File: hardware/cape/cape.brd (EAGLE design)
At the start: 86.4 x 54.6 mm, 159 parts, among them IC1 AD8422BRMZ, IC10 DAC8562_DGS_10, IC11 CAT24C256WI-GT3, IC12 LM27762DSSR, IC13 BQ25505, IC14 SN74LV4T125PWR, IC15 LMP7701MF, IC16 TXB0304RUTR, IC2 OPA2388DGK8_L, IC3 AD8422BRMZ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

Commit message: hardware: fixed wrong part number for constant supply LDO
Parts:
- IC8: value TPS73125DBVR -> TPS73101DBVR; device mylib:SOT95P280X145-5N -> shepherd:SOT95P280X145-5N
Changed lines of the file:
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@@
 <attribute name="VALUE" x="29.591" y="21.442" size="1.27" layer="27" rot="R180" align="top-center"/>
 </element>
-<element name="IC8" library="mylib" package="SOT95P280X145-5N" value="TPS73125DBVR" x="49.403" y="33.782" smashed="yes" rot="R180">
+<element name="IC8" library="shepherd" package="SOT95P280X145-5N" value="TPS73101DBVR" x="49.403" y="33.782" smashed="yes" rot="R180">
 <attribute name="AVAILABILITY" value="Unavailable" x="49.403" y="33.782" size="1.778" layer="27" rot="R180" display="off"/>
 <attribute name="DESCRIPTION" value=" Cap-Free, NMOS, 150mA Low Dropout Regulator with Reverse Current Protection 5-SOT-23 -40 to 125 " x="49.403" y="33.782" size="1.778" layer="27" rot="R180" display="off"/>
 <attribute name="MF" value="Texas Instruments" x="49.403" y="33.782" size="1.778" layer="27" rot="R180" display="off"/>
-<attribute name="MP" value="TPS73125DBVR" x="49.403" y="33.782" size="1.778" layer="27" rot="R180" display="off"/>
+<attribute name="MP" value="TPS73101DBVR" x="49.403" y="33.782" size="1.778" layer="27" rot="R180" display="off"/>
 <attribute name="NAME" x="49.62795" y="35.435690625" size="0.8128" layer="25" font="vector" ratio="15" rot="SR0"/>
 <attribute name="PACKAGE" value="SOT-23-5 Texas Instruments" x="49.403" y="33.782" size="1.778" layer="27" rot="R180" display="off"/>

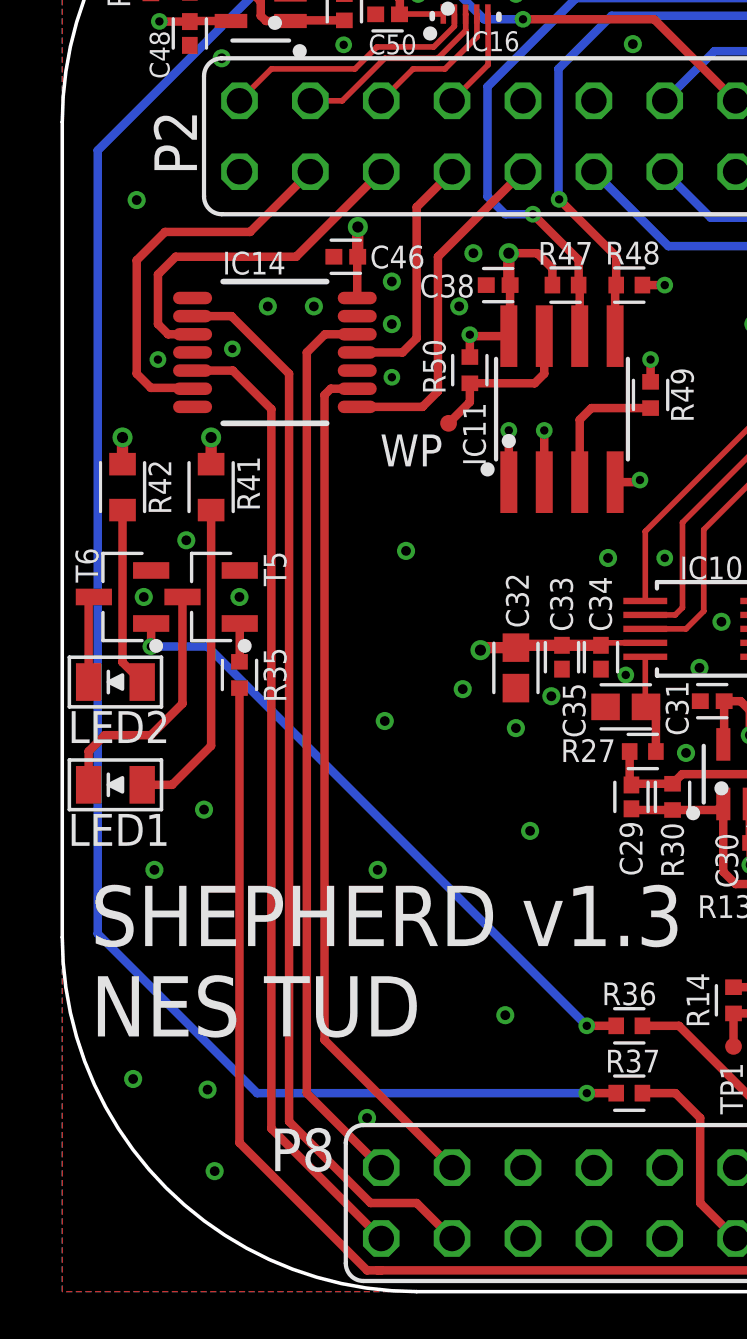
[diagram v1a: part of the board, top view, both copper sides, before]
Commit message: hardware: fixed direction of level-converter
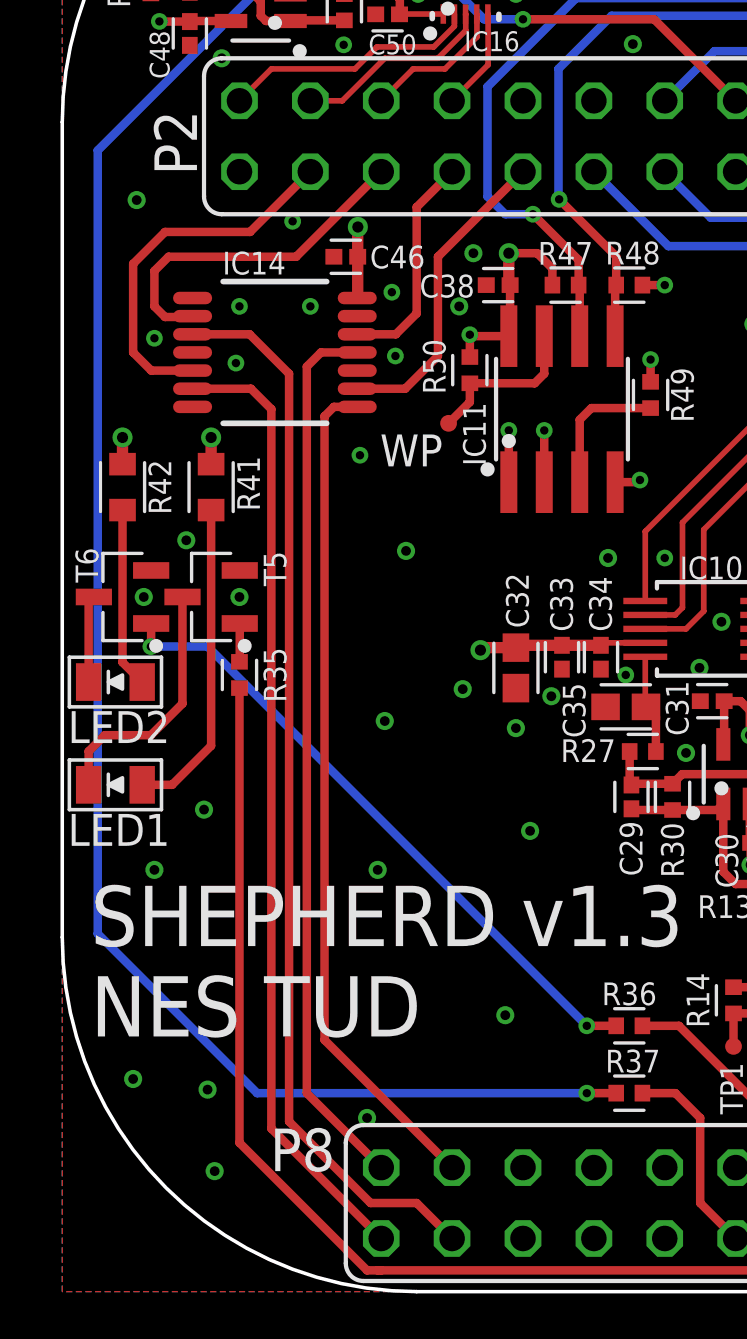
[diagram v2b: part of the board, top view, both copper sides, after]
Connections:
- net GPIO0_BB: now also IC14.11; no longer IC14.12
- net GPIO0_TARGET: now also IC14.12; no longer IC14.11
- net GPIO1_BB: now also IC14.6; no longer IC14.5
- net GPIO1_TARGET: now also IC14.5; no longer IC14.6
- net GPIO2_BB: now also IC14.8; no longer IC14.9
- net GPIO2_TARGET: now also IC14.9; no longer IC14.8
- net GPIO3_BB: now also IC14.3; no longer IC14.2
- net GPIO3_TARGET: now also IC14.2; no longer IC14.3
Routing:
- net GPIO2_TARGET: track 12.3 -> 11.2 mm
- net GPIO0_TARGET: track 8.84 -> 8.05 mm
- net GPIO2_BB: track 30.8 -> 30.1 mm
- net GPIO0_BB: track 32.4 -> 31.8 mm
- net GPIO1_TARGET: track 13.8 -> 13.3 mm
- net GND: vias 154 -> 155
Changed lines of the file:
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@@
 <via x="32.131" y="21.971" extent="1-16" drill="0.35"/>
 <via x="25.654" y="27.051" extent="1-16" drill="0.35" alwaysstop="yes"/>
-<via x="9.017" y="35.306" extent="1-16" drill="0.35"/>
-<via x="7.366" y="35.306" extent="1-16" drill="0.35"/>
-<via x="11.811" y="36.195" extent="1-16" drill="0.35"/>
-<via x="11.811" y="34.671" extent="1-16" drill="0.35"/>
 <via x="20.447" y="44.704" extent="1-16" drill="0.35"/>
 <via x="29.083" y="36.195" extent="1-16" drill="0.35"/>
@@
 <via x="57.912" y="15.24" extent="1-16" drill="0.3"/>
 <via x="60.96" y="15.24" extent="1-16" drill="0.3"/>
-<via x="3.429" y="33.401" extent="1-16" drill="0.3"/>
-<via x="11.811" y="32.766" extent="1-16" drill="0.3"/>
-<via x="6.096" y="33.782" extent="1-16" drill="0.3"/>
 <via x="6.35" y="24.892" extent="1-16" drill="0.35"/>
 <via x="2.921" y="24.892" extent="1-16" drill="0.35"/>
@@
 <via x="9.3218" y="49.911" extent="1-16" drill="0.3"/>
 <via x="5.715" y="44.196" extent="1-16" drill="0.35"/>
+<via x="6.35" y="35.306" extent="1-16" drill="0.3"/>
+<via x="8.89" y="35.306" extent="1-16" drill="0.3"/>
+<via x="6.223" y="33.274" extent="1-16" drill="0.3"/>
+<via x="3.302" y="34.163" extent="1-16" drill="0.3"/>
+<via x="10.668" y="29.972" extent="1-16" drill="0.3"/>
+<via x="11.938" y="33.528" extent="1-16" drill="0.3"/>
+<via x="11.811" y="35.814" extent="1-16" drill="0.3"/>
+<via x="8.255" y="38.354" extent="1-16" drill="0.3"/>
 </signal>
 <signal name="V_H">
@@
 <contactref element="C46" pad="1"/>
 <contactref element="IC14" pad="14"/>
-<wire x1="10.57" y1="35.605" x2="10.57" y2="37.0671" width="0.3048" layer="1"/>
 <wire x1="10.57" y1="37.0671" x2="10.5869" y2="37.084" width="0.3048" layer="1"/>
 <wire x1="10.5869" y1="37.084" x2="10.5869" y2="38.1459" width="0.4064" layer="1"/>
@@
 <wire x1="12.0855" y1="48.6615" x2="12.7" y2="49.276" width="0.3048" layer="1"/>
 <via x="12.7" y="49.276" extent="1-16" drill="0.3"/>
+<wire x1="10.5869" y1="37.084" x2="10.5869" y2="35.6219" width="0.4064" layer="1"/>
+<wire x1="10.5869" y1="35.6219" x2="10.57" y2="35.605" width="0.4064" layer="1"/>
 </signal>
 <signal name="N$3">
@@
 <signal name="GPIO0_BB">
 <contactref element="P8" pad="45"/>
-<contactref element="IC14" pad="12"/>
-<wire x1="10.57" y1="34.305" x2="9.413" y2="34.305" width="0.3048" layer="1"/>
-<wire x1="8.763" y1="7.112" x2="11.43" y2="4.445" width="0.3048" layer="1"/>
-<wire x1="9.413" y1="34.305" x2="8.763" y2="33.655" width="0.3048" layer="1"/>
-<wire x1="8.763" y1="33.655" x2="8.763" y2="7.112" width="0.3048" layer="1"/>
+<wire x1="11.43" y1="4.445" x2="8.763" y2="7.112" width="0.3048" layer="1"/>
+<contactref element="IC14" pad="11"/>
+<wire x1="8.763" y1="7.112" x2="8.763" y2="33.147" width="0.3048" layer="1"/>
+<wire x1="8.763" y1="33.147" x2="9.271" y2="33.655" width="0.3048" layer="1"/>
+<wire x1="9.271" y1="33.655" x2="10.57" y2="33.655" width="0.3048" layer="1"/>
 </signal>
 <signal name="GPIO1_BB">
 <contactref element="P8" pad="46"/>
-<contactref element="IC14" pad="5"/>
 <wire x1="7.493" y1="5.842" x2="11.43" y2="1.905" width="0.3048" layer="1"/>
-<wire x1="4.669996875" y1="33.005" x2="6.111" y2="33.005" width="0.3048" layer="1"/>
-<wire x1="6.111" y1="33.005" x2="7.493" y2="31.623" width="0.3048" layer="1"/>
-<wire x1="7.493" y1="31.623" x2="7.493" y2="5.842" width="0.3048" layer="1"/>
+<wire x1="7.493" y1="5.842" x2="7.493" y2="31.623" width="0.3048" layer="1"/>
+<contactref element="IC14" pad="6"/>
+<wire x1="7.493" y1="31.623" x2="6.761" y2="32.355" width="0.3048" layer="1"/>
+<wire x1="6.761" y1="32.355" x2="4.669996875" y2="32.355" width="0.3048" layer="1"/>
 </signal>
 <signal name="GPIO2_BB">
 <contactref element="P8" pad="43"/>
-<contactref element="IC14" pad="9"/>
-<wire x1="9.622" y1="32.355" x2="10.57" y2="32.355" width="0.3048" layer="1"/>
 <wire x1="13.97" y1="4.445" x2="9.398" y2="9.017" width="0.3048" layer="1"/>
-<wire x1="9.398" y1="9.017" x2="9.398" y2="32.131" width="0.3048" layer="1"/>
-<wire x1="9.398" y1="32.131" x2="9.622" y2="32.355" width="0.3048" layer="1"/>
+<contactref element="IC14" pad="8"/>
+<wire x1="9.398" y1="9.017" x2="9.398" y2="31.369" width="0.3048" layer="1"/>
+<wire x1="9.734" y1="31.705" x2="10.57" y2="31.705" width="0.3048" layer="1"/>
+<wire x1="9.398" y1="31.369" x2="9.734" y2="31.705" width="0.3048" layer="1"/>
 </signal>
 <signal name="GPIO3_BB">
 <contactref element="P8" pad="44"/>
-<contactref element="IC14" pad="2"/>
-<wire x1="4.669996875" y1="34.955" x2="6.066" y2="34.955" width="0.3048" layer="1"/>
-<wire x1="6.066" y1="34.955" x2="8.128" y2="32.893" width="0.3048" layer="1"/>
 <wire x1="8.128" y1="6.096" x2="11.049" y2="3.175" width="0.3048" layer="1"/>
 <wire x1="11.049" y1="3.175" x2="12.7" y2="3.175" width="0.3048" layer="1"/>
 <wire x1="12.7" y1="3.175" x2="13.97" y2="1.905" width="0.3048" layer="1"/>
-<wire x1="8.128" y1="32.893" x2="8.128" y2="6.096" width="0.3048" layer="1"/>
+<wire x1="8.128" y1="6.096" x2="8.128" y2="32.893" width="0.3048" layer="1"/>
+<contactref element="IC14" pad="3"/>
+<wire x1="8.128" y1="32.893" x2="6.716" y2="34.305" width="0.3048" layer="1"/>
+<wire x1="6.716" y1="34.305" x2="4.669996875" y2="34.305" width="0.3048" layer="1"/>
 </signal>
 <signal name="GPIO0_TARGET">
 <contactref element="P2" pad="10"/>
-<contactref element="IC14" pad="11"/>
-<wire x1="10.57" y1="33.655" x2="12.192" y2="33.655" width="0.3048" layer="1"/>
-<wire x1="12.192" y1="33.655" x2="12.7" y2="34.163" width="0.3048" layer="1"/>
-<wire x1="12.7" y1="34.163" x2="12.7" y2="38.862" width="0.3048" layer="1"/>
-<wire x1="12.7" y1="38.862" x2="13.97" y2="40.132" width="0.3048" layer="1"/>
+<wire x1="13.97" y1="40.132" x2="12.7" y2="38.862" width="0.3048" layer="1"/>
+<contactref element="IC14" pad="12"/>
+<wire x1="11.953" y1="34.305" x2="10.57" y2="34.305" width="0.3048" layer="1"/>
+<wire x1="12.7" y1="38.862" x2="12.7" y2="35.052" width="0.3048" layer="1"/>
+<wire x1="12.7" y1="35.052" x2="11.953" y2="34.305" width="0.3048" layer="1"/>
 </signal>
 <signal name="GPIO1_TARGET">
 <contactref element="P2" pad="14"/>
-<contactref element="IC14" pad="6"/>
 <wire x1="8.89" y1="40.132" x2="6.731" y2="37.973" width="0.3048" layer="1"/>
-<wire x1="3.683" y1="37.973" x2="2.667" y2="36.957" width="0.3048" layer="1"/>
-<wire x1="2.667" y1="36.957" x2="2.667" y2="32.893" width="0.3048" layer="1"/>
-<wire x1="2.667" y1="32.893" x2="3.175" y2="32.385" width="0.3048" layer="1"/>
-<wire x1="3.175" y1="32.385" x2="4.639996875" y2="32.385" width="0.3048" layer="1"/>
-<wire x1="4.639996875" y1="32.385" x2="4.669996875" y2="32.355" width="0.3048" layer="1"/>
+<wire x1="3.683" y1="37.973" x2="2.54" y2="36.83" width="0.3048" layer="1"/>
 <wire x1="6.731" y1="37.973" x2="3.683" y2="37.973" width="0.3048" layer="1"/>
+<contactref element="IC14" pad="5"/>
+<wire x1="2.54" y1="36.83" x2="2.54" y2="33.655" width="0.3048" layer="1"/>
+<wire x1="3.19" y1="33.005" x2="4.669996875" y2="33.005" width="0.3048" layer="1"/>
+<wire x1="2.54" y1="33.655" x2="3.19" y2="33.005" width="0.3048" layer="1"/>
 </signal>
 <signal name="GPIO2_TARGET">
 <contactref element="P2" pad="8"/>
-<contactref element="IC14" pad="8"/>
-<wire x1="10.57" y1="31.705" x2="12.909" y2="31.705" width="0.3048" layer="1"/>
-<wire x1="12.909" y1="31.705" x2="13.462" y2="32.258" width="0.3048" layer="1"/>
-<wire x1="13.462" y1="32.258" x2="13.462" y2="37.084" width="0.3048" layer="1"/>
-<wire x1="13.462" y1="37.084" x2="16.51" y2="40.132" width="0.3048" layer="1"/>
+<wire x1="16.51" y1="40.132" x2="13.462" y2="37.084" width="0.3048" layer="1"/>
+<contactref element="IC14" pad="9"/>
+<wire x1="13.462" y1="37.084" x2="13.462" y2="33.528" width="0.3048" layer="1"/>
+<wire x1="13.462" y1="33.528" x2="12.289" y2="32.355" width="0.3048" layer="1"/>
+<wire x1="12.289" y1="32.355" x2="10.57" y2="32.355" width="0.3048" layer="1"/>
 </signal>
 <signal name="GPIO3_TARGET">
 <contactref element="P2" pad="12"/>
-<contactref element="IC14" pad="3"/>
-<wire x1="4.669996875" y1="34.305" x2="3.795" y2="34.305" width="0.3048" layer="1"/>
-<wire x1="3.795" y1="34.305" x2="3.429" y2="34.671" width="0.3048" layer="1"/>
-<wire x1="3.429" y1="34.671" x2="3.429" y2="36.449" width="0.3048" layer="1"/>
-<wire x1="3.429" y1="36.449" x2="4.064" y2="37.084" width="0.3048" layer="1"/>
-<wire x1="4.064" y1="37.084" x2="8.382" y2="37.084" width="0.3048" layer="1"/>
+<wire x1="3.302" y1="36.576" x2="3.81" y2="37.084" width="0.3048" layer="1"/>
+<wire x1="3.81" y1="37.084" x2="8.382" y2="37.084" width="0.3048" layer="1"/>
 <wire x1="8.382" y1="37.084" x2="11.43" y2="40.132" width="0.3048" layer="1"/>
+<contactref element="IC14" pad="2"/>
+<wire x1="3.302" y1="36.576" x2="3.302" y2="35.306" width="0.3048" layer="1"/>
+<wire x1="3.302" y1="35.306" x2="3.683" y2="34.925" width="0.3048" layer="1"/>
+<wire x1="3.683" y1="34.925" x2="4.639996875" y2="34.925" width="0.3048" layer="1"/>
+<wire x1="4.639996875" y1="34.925" x2="4.669996875" y2="34.955" width="0.3048" layer="1"/>
 </signal>
 <signal name="UART_RX_TARGET">

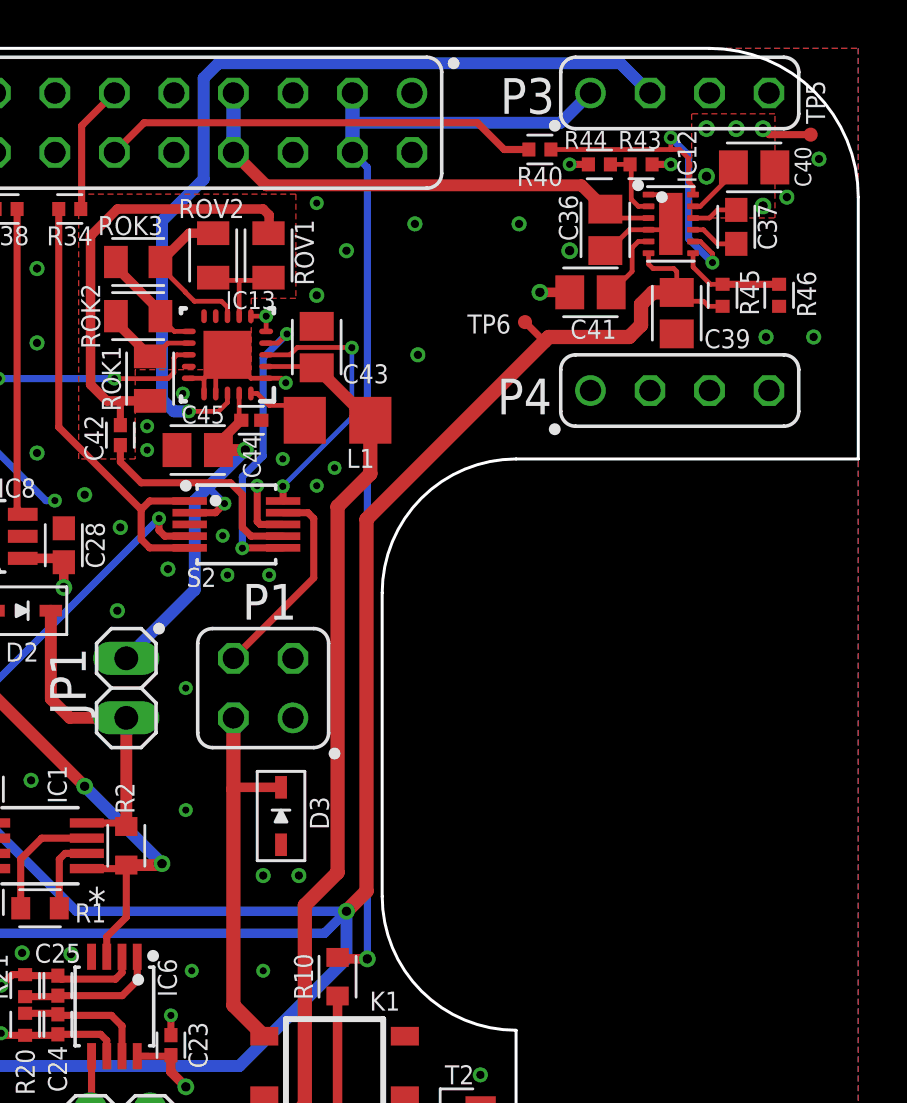
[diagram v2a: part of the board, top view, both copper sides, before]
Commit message: hardware: moved storage capelet to fit outline
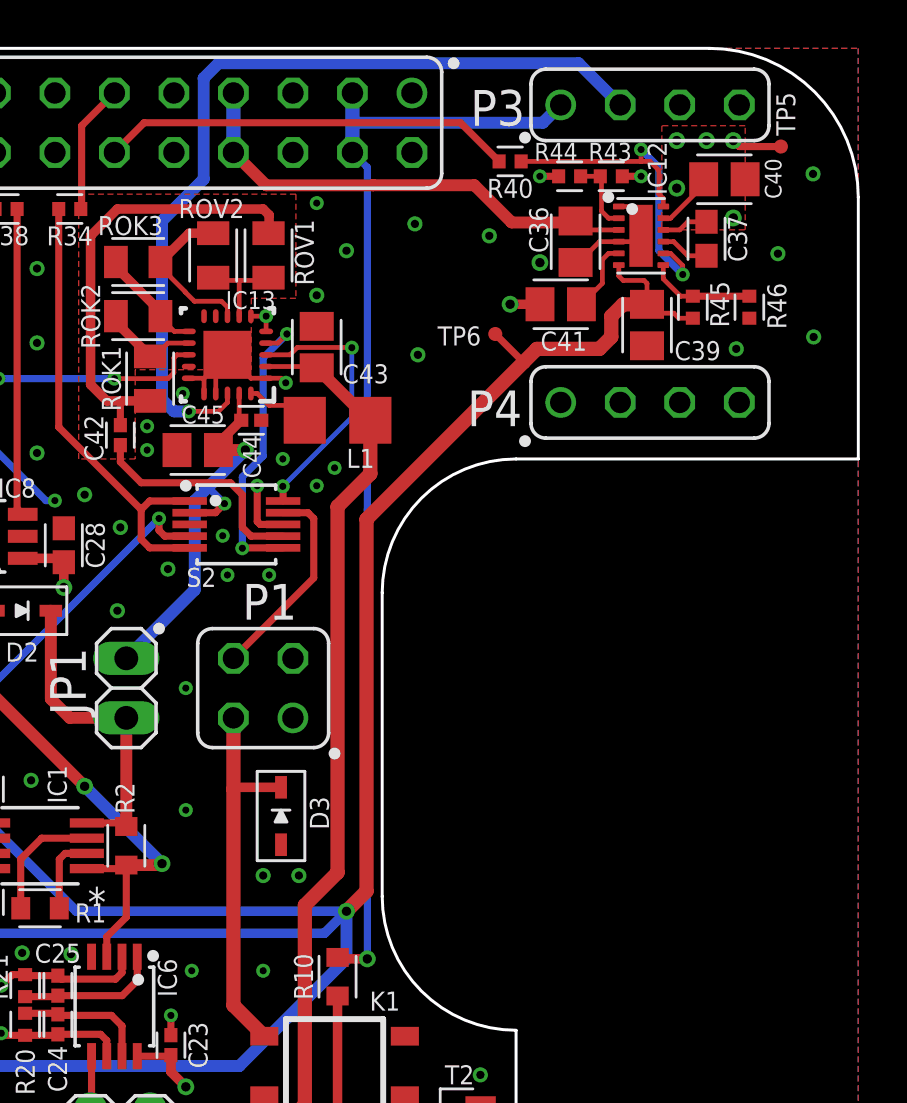
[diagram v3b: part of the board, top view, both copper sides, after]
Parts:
- moved C37 1.37 mm to (79.9, 46.5)
- moved C40 1.37 mm to (80.6, 49.0)
- moved R46 1.37 mm to (81.7, 43.6)
- moved C41 1.37 mm to (73.7, 43.7)
- moved R44 1.37 mm to (74.0, 49.1)
- moved C36 1.37 mm to (74.3, 46.4)
- moved C39 1.37 mm to (77.3, 42.8)
- moved P4 1.37 mm to (77.5, 39.5)
- moved R40 1.37 mm to (71.5, 49.8)
- moved R45 1.37 mm to (79.3, 43.6)
- moved TP5 1.37 mm to (83.1, 50.4)
- moved TP6 1.37 mm to (70.9, 42.4)
- moved IC12 1.37 mm to (77.1, 46.6)
- moved P3 1.37 mm to (77.5, 52.2)
- moved R43 1.37 mm to (75.8, 49.1)
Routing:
- net +3V3: track 81.6 -> 80.1 mm
- net V_BAT: track 37.8 -> 36.8 mm
- net N$103: track 18.7 -> 17.6 mm
- net +5V: track 21.4 -> 20.4 mm
- net VSS: track 129.5 -> 128.6 mm
